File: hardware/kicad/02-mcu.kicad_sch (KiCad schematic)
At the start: 4 parts, among them U1 ESP32-S3-N16R8

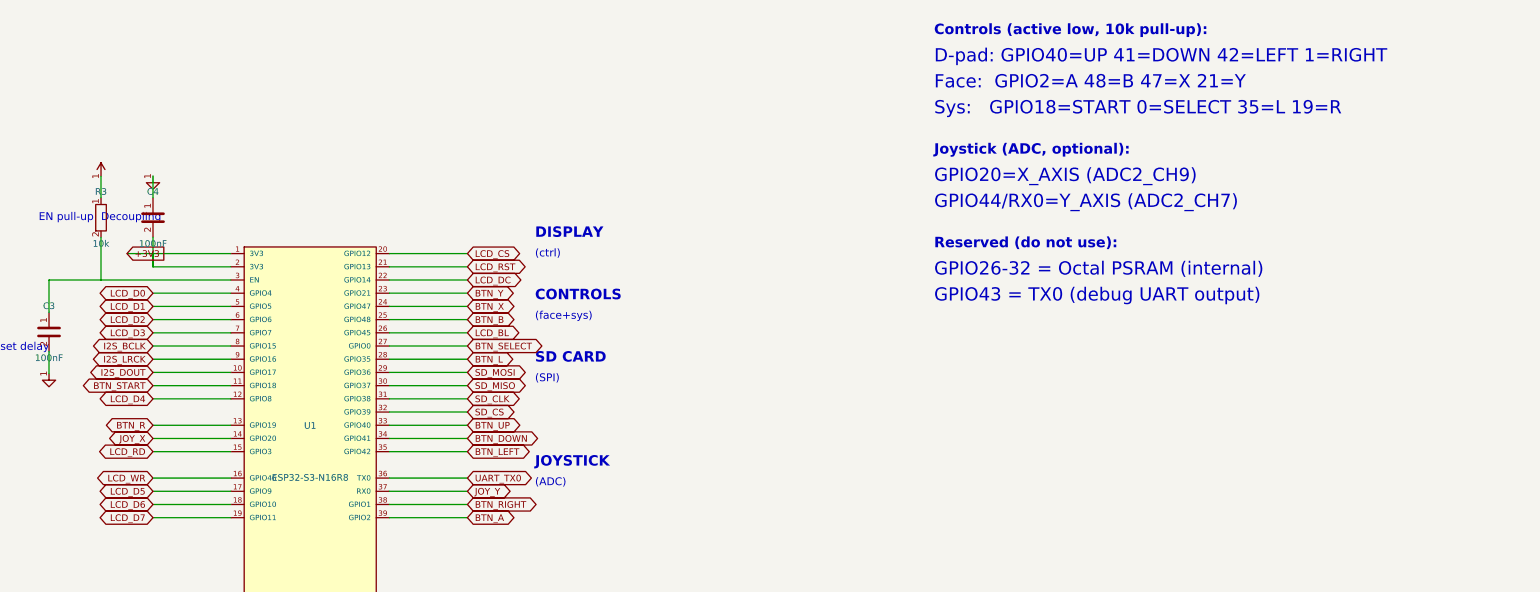
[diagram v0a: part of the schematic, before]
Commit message: Route USB D+/D- to ESP32-S3 GPIO19/20 for native firmware flashing
- Connect USB-C data lines to ESP32-S3 native USB pins (GPIO19=D-, GPIO20=D+)
- Relocate BTN_R from GPIO19 to GPIO43 (TX0, freed by USB replacing UART debug)
- Fix _PIN_TO_GPIO mapping bug: pins 36/37 → GPIO43/44, pins 38/39 → GPIO1/2
- Remove joystick (JOY_X/JOY_Y) — GPIO20 freed for USB, joystick needs both axes
- Increase FPC GND via drill 0.15→0.20mm / pad 0.40→0.45mm (avoid JLCPCB surcharge)
- Add 14 USB regression tests (pin mapping, trace routing, firmware sync, micro-via guard)
- Update all docs, schematics, firmware config, BOM/CPL, gerbers

DFM: 88/88 PASS | DFA: 9/9 PASS

Co-Authored-By: Claude Opus 4.6 <noreply@anthropic.com>
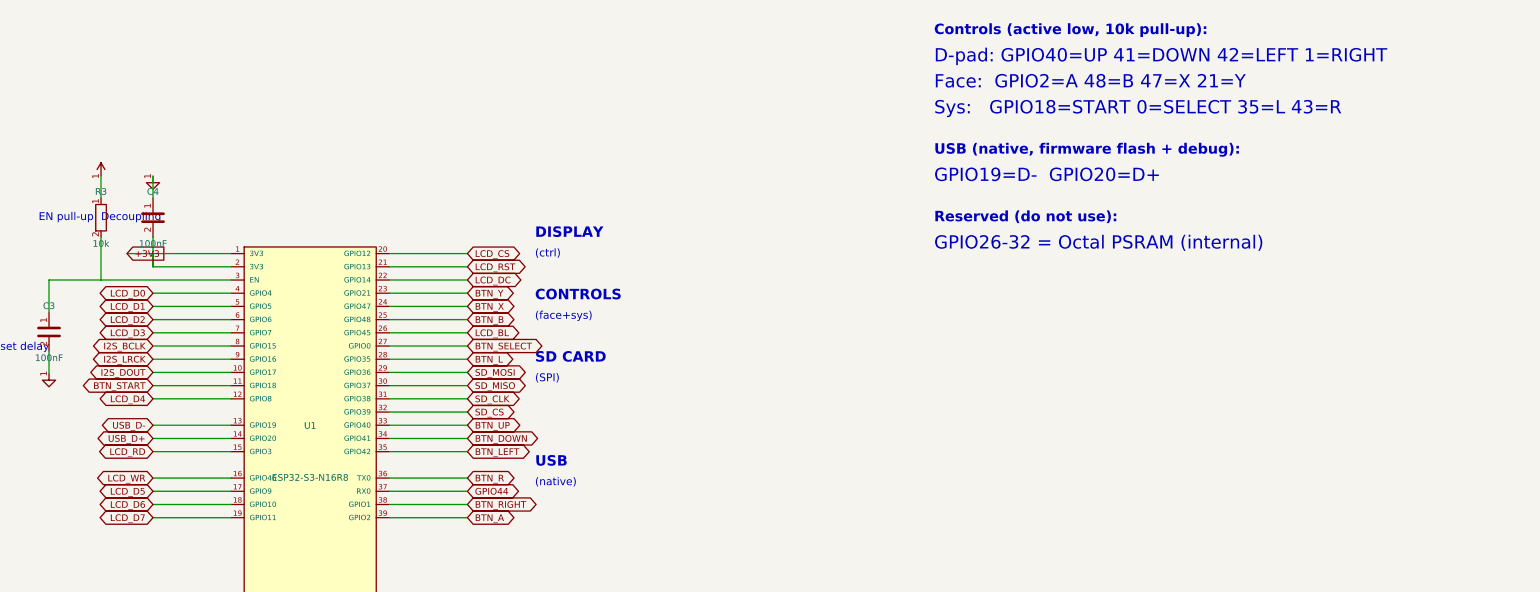
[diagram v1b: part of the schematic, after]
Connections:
- net UART_TX0 is gone; now on net BTN_R: U1.36 (TX0)
- net BTN_R: no longer U1.13 (GPIO19)
- net JOY_X renamed USB_D+
- net JOY_Y renamed GPIO44
- new net USB_D-: U1.13 (GPIO19)
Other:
- note added: "(native)"
- note added: "GPIO19=D- GPIO20=D+"
- note added: "Sys: GPIO18=START 0=SELECT 35=L 43=R"
- note added: "USB"
- note added: "USB (native, firmware flash + debug):"
- note removed: "(ADC)"
- note removed: "GPIO20=X_AXIS (ADC2_CH9)"
- note removed: "GPIO43 = TX0 (debug UART output)"
- note removed: "GPIO44/RX0=Y_AXIS (ADC2_CH7)"
- note removed: "JOYSTICK"
- note removed: "Joystick (ADC, optional):"
- note removed: "Sys: GPIO18=START 0=SELECT 35=L 19=R"
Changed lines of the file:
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@@
   (text "SD CARD" (at 243.24 152 0) (effects (font (size 2 2) bold) (justify left)))
   (text "(SPI)" (at 243.24 156 0) (effects (font (size 1.5 1.5)) (justify left)))
-  (text "JOYSTICK" (at 243.24 172 0) (effects (font (size 2 2) bold) (justify left)))
-  (text "(ADC)" (at 243.24 176 0) (effects (font (size 1.5 1.5)) (justify left)))
+  (text "USB" (at 243.24 172 0) (effects (font (size 2 2) bold) (justify left)))
+  (text "(native)" (at 243.24 176 0) (effects (font (size 1.5 1.5)) (justify left)))
   (wire (pts (xy 184.76 139.52) (xy 169.76 139.52)) (stroke (width 0) (type default)))
   (global_label "LCD_D0" (shape bidirectional) (at 169.76 139.52 180) (effects (font (size 1.27 1.27))) (property "Intersheetrefs" "" (at 0 0 0) (effects (font (size 1.27 1.27)) hide)))
@@
   (global_label "LCD_D4" (shape bidirectional) (at 169.76 159.84 180) (effects (font (size 1.27 1.27))) (property "Intersheetrefs" "" (at 0 0 0) (effects (font (size 1.27 1.27)) hide)))
   (wire (pts (xy 184.76 164.92) (xy 169.76 164.92)) (stroke (width 0) (type default)))
-  (global_label "BTN_R" (shape bidirectional) (at 169.76 164.92 180) (effects (font (size 1.27 1.27))) (property "Intersheetrefs" "" (at 0 0 0) (effects (font (size 1.27 1.27)) hide)))
+  (global_label "USB_D-" (shape bidirectional) (at 169.76 164.92 180) (effects (font (size 1.27 1.27))) (property "Intersheetrefs" "" (at 0 0 0) (effects (font (size 1.27 1.27)) hide)))
   (wire (pts (xy 184.76 167.46) (xy 169.76 167.46)) (stroke (width 0) (type default)))
-  (global_label "JOY_X" (shape bidirectional) (at 169.76 167.46 180) (effects (font (size 1.27 1.27))) (property "Intersheetrefs" "" (at 0 0 0) (effects (font (size 1.27 1.27)) hide)))
+  (global_label "USB_D+" (shape bidirectional) (at 169.76 167.46 180) (effects (font (size 1.27 1.27))) (property "Intersheetrefs" "" (at 0 0 0) (effects (font (size 1.27 1.27)) hide)))
   (wire (pts (xy 184.76 170) (xy 169.76 170)) (stroke (width 0) (type default)))
   (global_label "LCD_RD" (shape bidirectional) (at 169.76 170 180) (effects (font (size 1.27 1.27))) (property "Intersheetrefs" "" (at 0 0 0) (effects (font (size 1.27 1.27)) hide)))
@@
   (global_label "BTN_LEFT" (shape bidirectional) (at 230.24 170 0) (effects (font (size 1.27 1.27))) (property "Intersheetrefs" "" (at 0 0 0) (effects (font (size 1.27 1.27)) hide)))
   (wire (pts (xy 215.24 175.08) (xy 230.24 175.08)) (stroke (width 0) (type default)))
-  (global_label "UART_TX0" (shape bidirectional) (at 230.24 175.08 0) (effects (font (size 1.27 1.27))) (property "Intersheetrefs" "" (at 0 0 0) (effects (font (size 1.27 1.27)) hide)))
+  (global_label "BTN_R" (shape bidirectional) (at 230.24 175.08 0) (effects (font (size 1.27 1.27))) (property "Intersheetrefs" "" (at 0 0 0) (effects (font (size 1.27 1.27)) hide)))
   (wire (pts (xy 215.24 177.62) (xy 230.24 177.62)) (stroke (width 0) (type default)))
-  (global_label "JOY_Y" (shape bidirectional) (at 230.24 177.62 0) (effects (font (size 1.27 1.27))) (property "Intersheetrefs" "" (at 0 0 0) (effects (font (size 1.27 1.27)) hide)))
+  (global_label "GPIO44" (shape bidirectional) (at 230.24 177.62 0) (effects (font (size 1.27 1.27))) (property "Intersheetrefs" "" (at 0 0 0) (effects (font (size 1.27 1.27)) hide)))
   (wire (pts (xy 215.24 180.16) (xy 230.24 180.16)) (stroke (width 0) (type default)))
   (global_label "BTN_RIGHT" (shape bidirectional) (at 230.24 180.16 0) (effects (font (size 1.27 1.27))) (property "Intersheetrefs" "" (at 0 0 0) (effects (font (size 1.27 1.27)) hide)))
@@
   (text "D-pad: GPIO40=UP 41=DOWN 42=LEFT 1=RIGHT" (at 320 94 0) (effects (font (size 2.54 2.54)) (justify left)))
   (text "Face:  GPIO2=A 48=B 47=X 21=Y" (at 320 99 0) (effects (font (size 2.54 2.54)) (justify left)))
-  (text "Sys:   GPIO18=START 0=SELECT 35=L 19=R" (at 320 104 0) (effects (font (size 2.54 2.54)) (justify left)))
-  (text "Joystick (ADC, optional):" (at 320 112 0) (effects (font (size 2 2) bold) (justify left)))
-  (text "GPIO20=X_AXIS (ADC2_CH9)" (at 320 117 0) (effects (font (size 2.54 2.54)) (justify left)))
-  (text "GPIO44/RX0=Y_AXIS (ADC2_CH7)" (at 320 122 0) (effects (font (size 2.54 2.54)) (justify left)))
-  (text "Reserved (do not use):" (at 320 130 0) (effects (font (size 2 2) bold) (justify left)))
-  (text "GPIO26-32 = Octal PSRAM (internal)" (at 320 135 0) (effects (font (size 2.54 2.54)) (justify left)))
-  (text "GPIO43 = TX0 (debug UART output)" (at 320 140 0) (effects (font (size 2.54 2.54)) (justify left)))
+  (text "Sys:   GPIO18=START 0=SELECT 35=L 43=R" (at 320 104 0) (effects (font (size 2.54 2.54)) (justify left)))
+  (text "USB (native, firmware flash + debug):" (at 320 112 0) (effects (font (size 2 2) bold) (justify left)))
+  (text "GPIO19=D-  GPIO20=D+" (at 320 117 0) (effects (font (size 2.54 2.54)) (justify left)))
+  (text "Reserved (do not use):" (at 320 125 0) (effects (font (size 2 2) bold) (justify left)))
+  (text "GPIO26-32 = Octal PSRAM (internal)" (at 320 130 0) (effects (font (size 2.54 2.54)) (justify left)))
   (sheet_instances (path "/" (page "2")))
 )

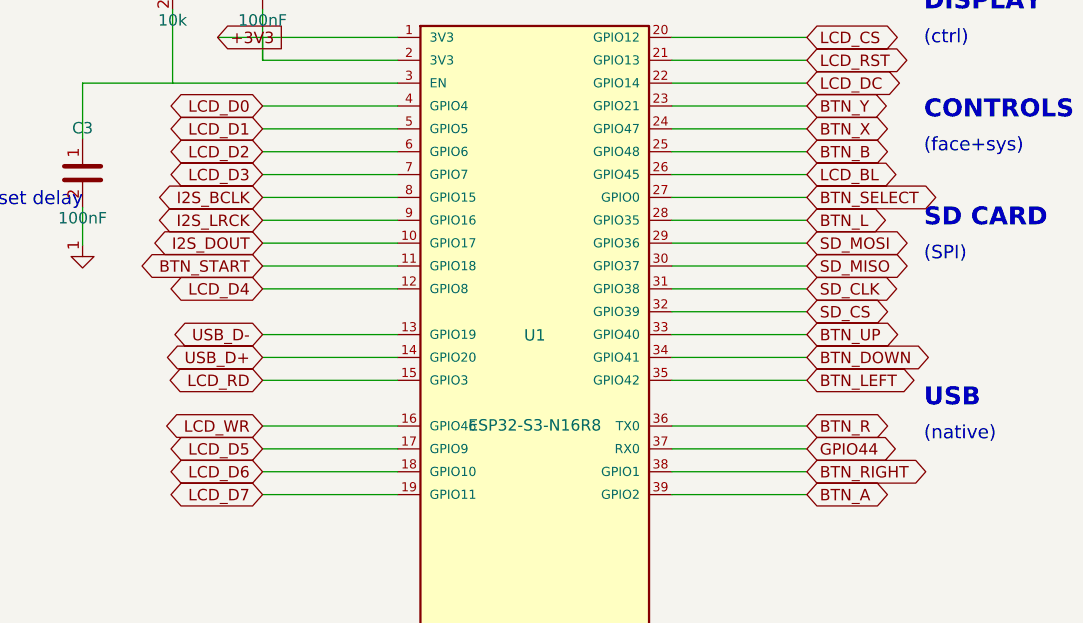
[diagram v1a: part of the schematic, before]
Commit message: fix(schematic): add 7 PAM8403 passives to audio sheet (C21-C25, R20-R21)
Components were in PCB/BOM/CPL but missing from schematic, causing
verify_schematic_pcb.py to report FAIL. All 71 JLCPCB components now
have matching schematic symbols (coverage PASS).

Co-Authored-By: Claude Opus 4.6 (1M context) <noreply@anthropic.com>
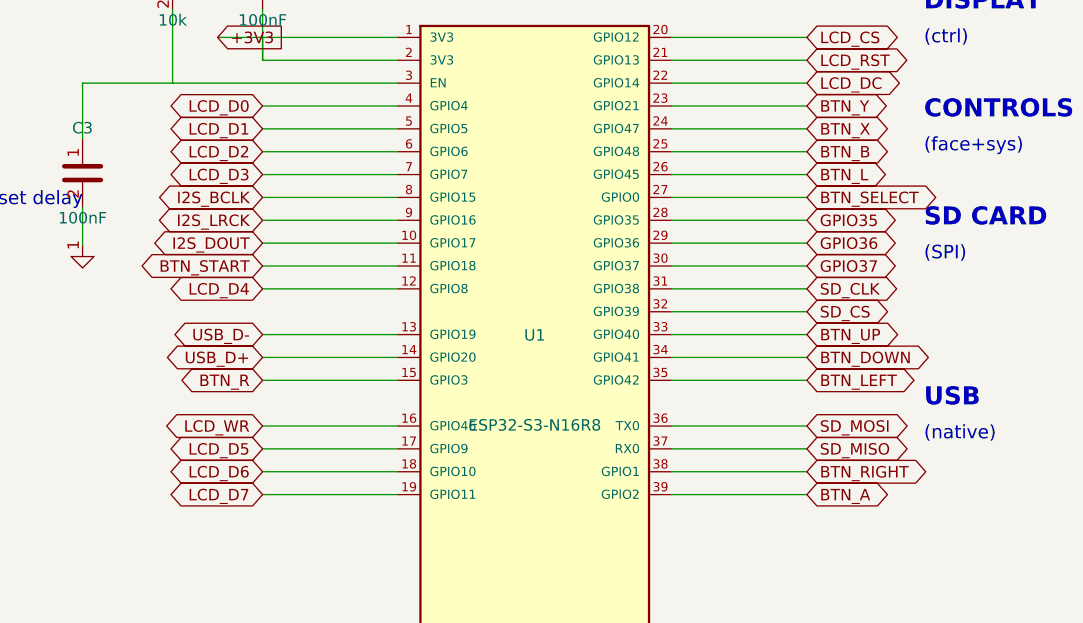
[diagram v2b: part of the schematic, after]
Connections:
- net GPIO44 is gone; now on net SD_MISO: U1.37 (RX0)
- net LCD_BL is gone; now on net BTN_L: U1.26 (GPIO45)
- net LCD_RD is gone; now on net BTN_R: U1.15 (GPIO3)
- net BTN_L: no longer U1.28 (GPIO35)
- net BTN_R: no longer U1.36 (TX0)
- net SD_MISO: no longer U1.30 (GPIO37)
- net SD_MOSI: now also U1.36 (TX0); no longer U1.29 (GPIO36)
- new net GPIO35: U1.28 (GPIO35)
- new net GPIO36: U1.29 (GPIO36)
- new net GPIO37: U1.30 (GPIO37)
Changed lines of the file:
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@@
   (global_label "USB_D+" (shape bidirectional) (at 169.76 167.46 180) (effects (font (size 1.27 1.27))) (property "Intersheetrefs" "" (at 0 0 0) (effects (font (size 1.27 1.27)) hide)))
   (wire (pts (xy 184.76 170) (xy 169.76 170)) (stroke (width 0) (type default)))
-  (global_label "LCD_RD" (shape bidirectional) (at 169.76 170 180) (effects (font (size 1.27 1.27))) (property "Intersheetrefs" "" (at 0 0 0) (effects (font (size 1.27 1.27)) hide)))
+  (global_label "BTN_R" (shape bidirectional) (at 169.76 170 180) (effects (font (size 1.27 1.27))) (property "Intersheetrefs" "" (at 0 0 0) (effects (font (size 1.27 1.27)) hide)))
   (wire (pts (xy 184.76 175.08) (xy 169.76 175.08)) (stroke (width 0) (type default)))
   (global_label "LCD_WR" (shape bidirectional) (at 169.76 175.08 180) (effects (font (size 1.27 1.27))) (property "Intersheetrefs" "" (at 0 0 0) (effects (font (size 1.27 1.27)) hide)))
@@
   (global_label "BTN_B" (shape bidirectional) (at 230.24 144.6 0) (effects (font (size 1.27 1.27))) (property "Intersheetrefs" "" (at 0 0 0) (effects (font (size 1.27 1.27)) hide)))
   (wire (pts (xy 215.24 147.14) (xy 230.24 147.14)) (stroke (width 0) (type default)))
-  (global_label "LCD_BL" (shape bidirectional) (at 230.24 147.14 0) (effects (font (size 1.27 1.27))) (property "Intersheetrefs" "" (at 0 0 0) (effects (font (size 1.27 1.27)) hide)))
+  (global_label "BTN_L" (shape bidirectional) (at 230.24 147.14 0) (effects (font (size 1.27 1.27))) (property "Intersheetrefs" "" (at 0 0 0) (effects (font (size 1.27 1.27)) hide)))
   (wire (pts (xy 215.24 149.68) (xy 230.24 149.68)) (stroke (width 0) (type default)))
   (global_label "BTN_SELECT" (shape bidirectional) (at 230.24 149.68 0) (effects (font (size 1.27 1.27))) (property "Intersheetrefs" "" (at 0 0 0) (effects (font (size 1.27 1.27)) hide)))
   (wire (pts (xy 215.24 152.22) (xy 230.24 152.22)) (stroke (width 0) (type default)))
-  (global_label "BTN_L" (shape bidirectional) (at 230.24 152.22 0) (effects (font (size 1.27 1.27))) (property "Intersheetrefs" "" (at 0 0 0) (effects (font (size 1.27 1.27)) hide)))
+  (global_label "GPIO35" (shape bidirectional) (at 230.24 152.22 0) (effects (font (size 1.27 1.27))) (property "Intersheetrefs" "" (at 0 0 0) (effects (font (size 1.27 1.27)) hide)))
   (wire (pts (xy 215.24 154.76) (xy 230.24 154.76)) (stroke (width 0) (type default)))
-  (global_label "SD_MOSI" (shape bidirectional) (at 230.24 154.76 0) (effects (font (size 1.27 1.27))) (property "Intersheetrefs" "" (at 0 0 0) (effects (font (size 1.27 1.27)) hide)))
+  (global_label "GPIO36" (shape bidirectional) (at 230.24 154.76 0) (effects (font (size 1.27 1.27))) (property "Intersheetrefs" "" (at 0 0 0) (effects (font (size 1.27 1.27)) hide)))
   (wire (pts (xy 215.24 157.3) (xy 230.24 157.3)) (stroke (width 0) (type default)))
-  (global_label "SD_MISO" (shape bidirectional) (at 230.24 157.3 0) (effects (font (size 1.27 1.27))) (property "Intersheetrefs" "" (at 0 0 0) (effects (font (size 1.27 1.27)) hide)))
+  (global_label "GPIO37" (shape bidirectional) (at 230.24 157.3 0) (effects (font (size 1.27 1.27))) (property "Intersheetrefs" "" (at 0 0 0) (effects (font (size 1.27 1.27)) hide)))
   (wire (pts (xy 215.24 159.84) (xy 230.24 159.84)) (stroke (width 0) (type default)))
   (global_label "SD_CLK" (shape bidirectional) (at 230.24 159.84 0) (effects (font (size 1.27 1.27))) (property "Intersheetrefs" "" (at 0 0 0) (effects (font (size 1.27 1.27)) hide)))
@@
   (global_label "BTN_LEFT" (shape bidirectional) (at 230.24 170 0) (effects (font (size 1.27 1.27))) (property "Intersheetrefs" "" (at 0 0 0) (effects (font (size 1.27 1.27)) hide)))
   (wire (pts (xy 215.24 175.08) (xy 230.24 175.08)) (stroke (width 0) (type default)))
-  (global_label "BTN_R" (shape bidirectional) (at 230.24 175.08 0) (effects (font (size 1.27 1.27))) (property "Intersheetrefs" "" (at 0 0 0) (effects (font (size 1.27 1.27)) hide)))
+  (global_label "SD_MOSI" (shape bidirectional) (at 230.24 175.08 0) (effects (font (size 1.27 1.27))) (property "Intersheetrefs" "" (at 0 0 0) (effects (font (size 1.27 1.27)) hide)))
   (wire (pts (xy 215.24 177.62) (xy 230.24 177.62)) (stroke (width 0) (type default)))
-  (global_label "GPIO44" (shape bidirectional) (at 230.24 177.62 0) (effects (font (size 1.27 1.27))) (property "Intersheetrefs" "" (at 0 0 0) (effects (font (size 1.27 1.27)) hide)))
+  (global_label "SD_MISO" (shape bidirectional) (at 230.24 177.62 0) (effects (font (size 1.27 1.27))) (property "Intersheetrefs" "" (at 0 0 0) (effects (font (size 1.27 1.27)) hide)))
   (wire (pts (xy 215.24 180.16) (xy 230.24 180.16)) (stroke (width 0) (type default)))
   (global_label "BTN_RIGHT" (shape bidirectional) (at 230.24 180.16 0) (effects (font (size 1.27 1.27))) (property "Intersheetrefs" "" (at 0 0 0) (effects (font (size 1.27 1.27)) hide)))
